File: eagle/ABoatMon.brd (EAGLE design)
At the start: 78.7 x 61 mm, 29 parts, among them J1 5V, J2 GND, J3 GND, J4 5V, X1 MKDSN1,5/3-5,08, X6 MKDSN1,5/3-5,08

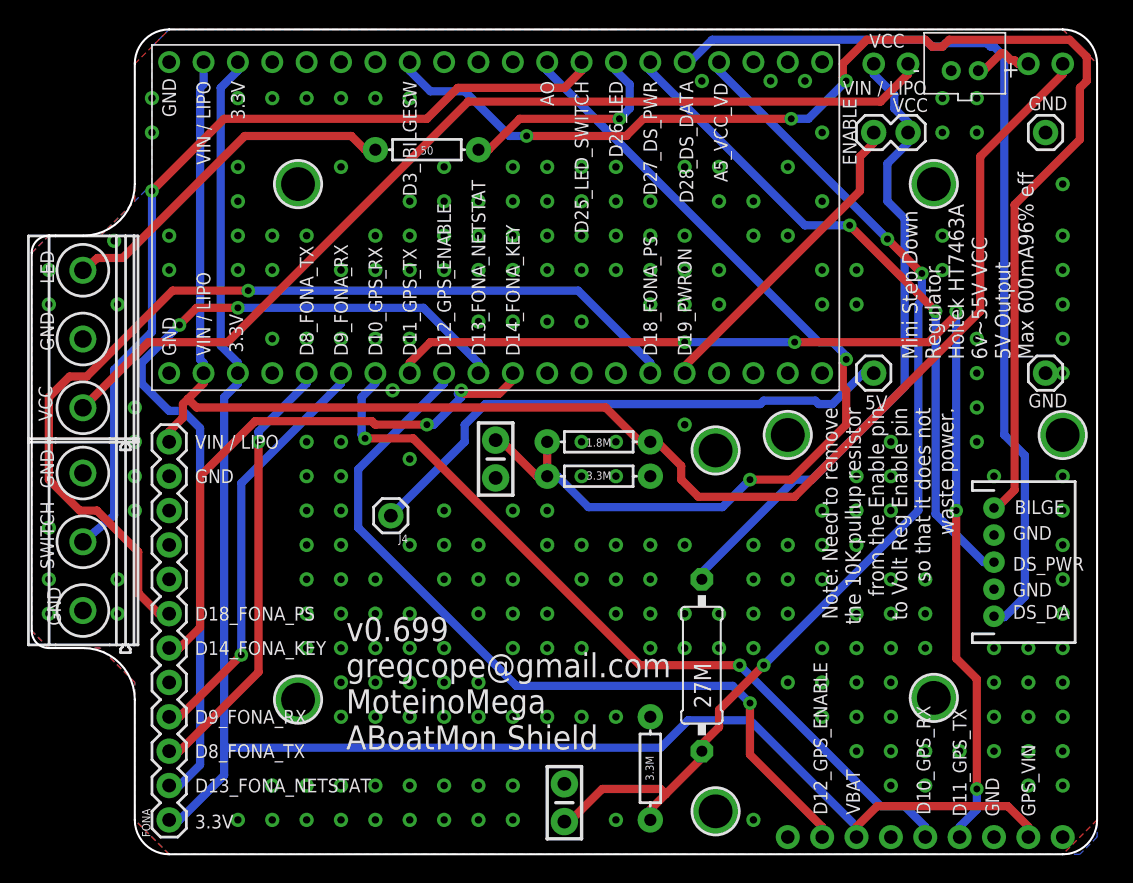
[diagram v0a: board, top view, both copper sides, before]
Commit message: Moved boxmounting holes 3mm
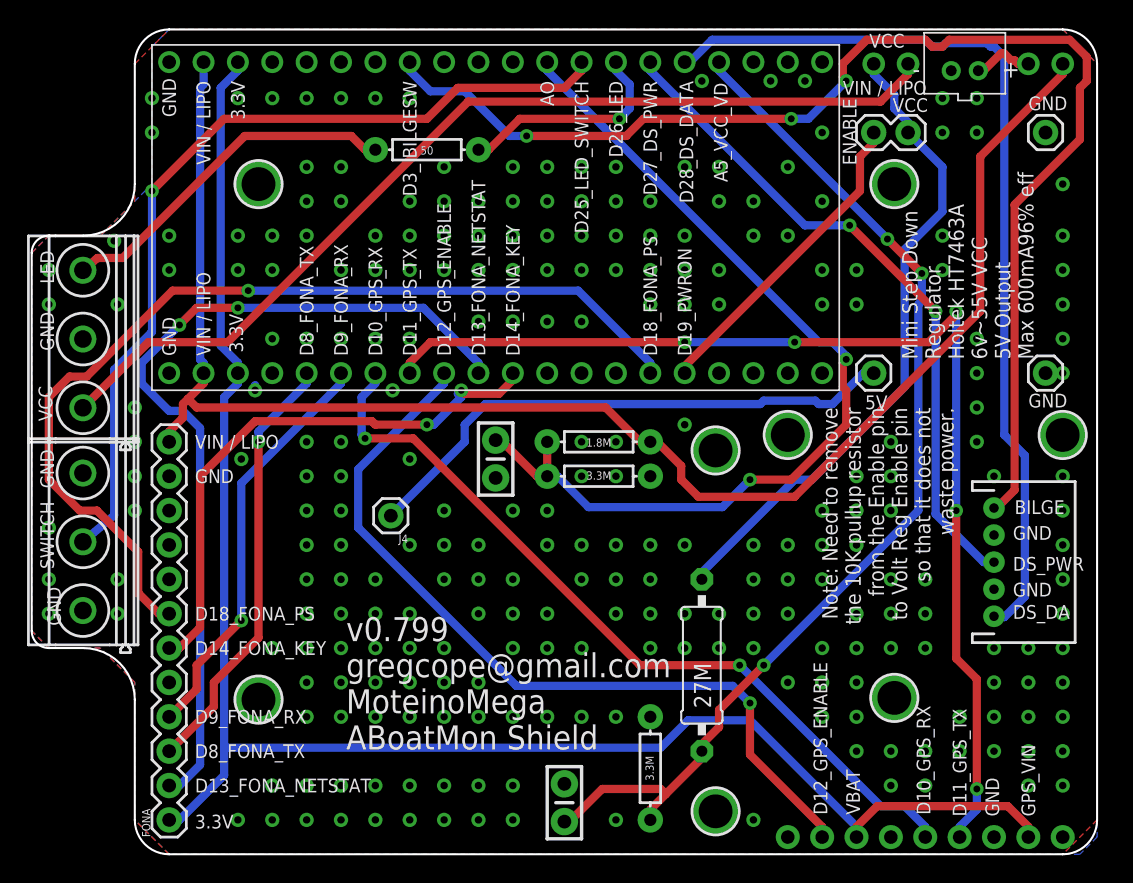
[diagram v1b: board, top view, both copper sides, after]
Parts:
- moved U$1 2.92 mm to (18.0, 11.4)
- moved U$6 2.92 mm to (18.0, 49.5)
- moved U$7 2.92 mm to (65.0, 49.5)
- moved U$8 2.92 mm to (65.0, 11.6)
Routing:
- net VCC_JUMPER: track 47.3 -> 48.3 mm
- net GND: track 0.00 -> 0.38 mm, vias 258 -> 257
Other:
- board text added: "v0.799 gregcope@gmail.com MoteinoMega ABoatMon Shield"
- board text removed: "v0.699 gregcope@gmail.com MoteinoMega ABoatMon Shield"
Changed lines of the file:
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@@
 <dimension x1="63.5" y1="35.56" x2="76.2" y2="35.56" x3="69.85" y3="34.29" textsize="1.778" layer="25"/>
 <dimension x1="63.5" y1="35.56" x2="63.5" y2="53.34" x3="63.881" y3="44.45" textsize="1.778" layer="25"/>
-<text x="24.511" y="7.747" size="1.778" layer="25">v0.699
+<text x="24.511" y="7.747" size="1.778" layer="25">v0.799
 gregcope@gmail.com
 MoteinoMega
@@
 <wire x1="77.47" y1="0" x2="80.01" y2="2.54" width="0.1524" layer="20" curve="90"/>
 <text x="73.787" y="19.05" size="1.016" layer="25" font="vector" ratio="20">GND</text>
+<dimension x1="20.955" y1="49.53" x2="18.034" y2="49.53" x3="19.4945" y3="9.779" textsize="1.778" layer="25"/>
 </plain>
 <attributes>
@@
 <attribute name="VALUE" x="74.803" y="23.241" size="0.6096" layer="27" font="vector" ratio="20" rot="R270"/>
 </element>
-<element name="U$1" library="microbuilder" package="MOUNTINGHOLE_2.5_PLATED" value="MOUNTINGHOLE2.5" x="20.955" y="11.43" smashed="yes"/>
-<element name="U$6" library="microbuilder" package="MOUNTINGHOLE_2.5_PLATED" value="MOUNTINGHOLE2.5" x="20.955" y="49.53" smashed="yes"/>
-<element name="U$7" library="microbuilder" package="MOUNTINGHOLE_2.5_PLATED" value="MOUNTINGHOLE2.5" x="67.945" y="49.53" smashed="yes"/>
-<element name="U$8" library="microbuilder" package="MOUNTINGHOLE_2.5_PLATED" value="MOUNTINGHOLE2.5" x="67.945" y="11.557" smashed="yes"/>
+<element name="U$1" library="microbuilder" package="MOUNTINGHOLE_2.5_PLATED" value="MOUNTINGHOLE2.5" x="18.034" y="11.43" smashed="yes"/>
+<element name="U$6" library="microbuilder" package="MOUNTINGHOLE_2.5_PLATED" value="MOUNTINGHOLE2.5" x="18.034" y="49.53" smashed="yes"/>
+<element name="U$7" library="microbuilder" package="MOUNTINGHOLE_2.5_PLATED" value="MOUNTINGHOLE2.5" x="65.024" y="49.53" smashed="yes"/>
+<element name="U$8" library="microbuilder" package="MOUNTINGHOLE_2.5_PLATED" value="MOUNTINGHOLE2.5" x="65.024" y="11.557" smashed="yes"/>
 </elements>
 <signals>
@@
 <via x="7.62" y="20.32" extent="1-16" drill="0.55"/>
 <via x="11.43" y="45.72" extent="1-16" drill="0.55"/>
-<via x="16.51" y="50.8" extent="1-16" drill="0.55"/>
-<via x="16.51" y="48.26" extent="1-16" drill="0.55"/>
 <via x="16.51" y="45.72" extent="1-16" drill="0.55"/>
 <via x="16.51" y="43.18" extent="1-16" drill="0.55"/>
@@
 <via x="59.69" y="12.7" extent="1-16" drill="0.55"/>
 <via x="62.23" y="12.7" extent="1-16" drill="0.55"/>
-<via x="64.77" y="12.7" extent="1-16" drill="0.55"/>
 <via x="59.69" y="10.16" extent="1-16" drill="0.55"/>
 <via x="62.23" y="10.16" extent="1-16" drill="0.55"/>
-<via x="64.77" y="10.16" extent="1-16" drill="0.55"/>
 <via x="62.23" y="7.62" extent="1-16" drill="0.55"/>
 <via x="64.77" y="7.62" extent="1-16" drill="0.55"/>
@@
 <via x="71.12" y="33.02" extent="1-16" drill="0.55"/>
 <via x="71.12" y="30.48" extent="1-16" drill="0.55"/>
-<wire x1="27.94" y1="34.29" x2="26.67" y2="38.1" width="0" layer="19" extent="1-1"/>
+<via x="69.85" y="10.16" extent="1-16" drill="0.55"/>
+<via x="17.78" y="34.29" extent="1-16" drill="0.55"/>
+<via x="16.764" y="29.21" extent="1-16" drill="0.55"/>
+<wire x1="17.78" y1="34.29" x2="17.78" y2="34.6747375" width="0.6096" layer="16"/>
+<wire x1="17.78" y1="34.6747375" x2="17.78" y2="34.6747375" width="0.6096" layer="16"/>
+<wire x1="17.78" y1="34.6747375" x2="19.05" y2="38.1" width="0" layer="19" extent="16-16"/>
 </signal>
 <signal name="VIN" class="1">
@@
 <contactref element="FONA" pad="4"/>
 <wire x1="24.13" y1="34.798" x2="24.13" y2="35.56" width="0.6096" layer="16"/>
-<wire x1="16.764" y1="27.432" x2="24.13" y2="34.798" width="0.6096" layer="16"/>
-<wire x1="16.764" y1="14.732" x2="16.764" y2="27.432" width="0.6096" layer="16"/>
-<wire x1="12.192" y1="10.16" x2="16.764" y2="14.732" width="0.6096" layer="1"/>
-<wire x1="11.43" y1="10.16" x2="12.192" y2="10.16" width="0.6096" layer="1"/>
-<via x="16.764" y="14.732" extent="1-16" drill="0.508"/>
+<wire x1="24.13" y1="34.798" x2="16.764" y2="27.432" width="0.6096" layer="16"/>
+<wire x1="16.764" y1="17.272" x2="13.462" y2="13.97" width="0.6096" layer="1"/>
+<wire x1="13.462" y1="13.97" x2="13.462" y2="12.192" width="0.6096" layer="1"/>
+<wire x1="11.43" y1="10.16" x2="13.462" y2="12.192" width="0.6096" layer="1"/>
+<via x="16.764" y="17.272" extent="1-16" drill="0.508"/>
+<wire x1="16.764" y1="27.432" x2="16.764" y2="17.272" width="0.6096" layer="16"/>
 </signal>
 <signal name="D8_FONA_TX">
@@
 <wire x1="18.034" y1="31.242" x2="21.59" y2="34.798" width="0.6096" layer="16"/>
 <wire x1="18.034" y1="30.48" x2="18.034" y2="31.242" width="0.6096" layer="16"/>
-<wire x1="18.034" y1="13.462" x2="18.034" y2="30.48" width="0.6096" layer="1"/>
-<wire x1="12.192" y1="7.62" x2="18.034" y2="13.462" width="0.6096" layer="1"/>
-<wire x1="11.43" y1="7.62" x2="12.192" y2="7.62" width="0.6096" layer="1"/>
+<wire x1="18.034" y1="16.002" x2="18.034" y2="30.48" width="0.6096" layer="1"/>
+<wire x1="18.034" y1="16.002" x2="14.732" y2="12.7" width="0.6096" layer="1"/>
+<wire x1="14.732" y1="12.7" x2="14.732" y2="10.922" width="0.6096" layer="1"/>
+<wire x1="11.43" y1="7.62" x2="14.732" y2="10.922" width="0.6096" layer="1"/>
 <via x="18.034" y="30.48" extent="1-16" drill="0.508"/>
 </signal>
@@
 <wire x1="58.928" y1="27.686" x2="57.658" y2="27.686" width="0.6096" layer="16"/>
 <wire x1="65.786" y1="34.544" x2="58.928" y2="27.686" width="0.6096" layer="16"/>
-<wire x1="65.786" y1="46.99" x2="65.786" y2="34.544" width="0.6096" layer="16"/>
-<wire x1="64.516" y1="48.26" x2="65.786" y2="46.99" width="0.6096" layer="16"/>
-<wire x1="64.516" y1="51.054" x2="64.516" y2="48.26" width="0.6096" layer="16"/>
-<wire x1="66.04" y1="52.578" x2="64.516" y2="51.054" width="0.6096" layer="16"/>
-<wire x1="66.04" y1="53.34" x2="66.04" y2="52.578" width="0.6096" layer="16"/>
+<wire x1="65.786" y1="44.704" x2="65.786" y2="34.544" width="0.6096" layer="16"/>
+<wire x1="68.58" y1="47.498" x2="65.786" y2="44.704" width="0.6096" layer="16"/>
+<wire x1="66.04" y1="53.34" x2="68.58" y2="50.8" width="0.6096" layer="16"/>
+<wire x1="68.58" y1="50.8" x2="68.58" y2="47.498" width="0.6096" layer="16"/>
 <wire x1="63.5" y1="57.658" x2="63.5" y2="58.42" width="0.6096" layer="16"/>
 <wire x1="65.024" y1="56.134" x2="63.5" y2="57.658" width="0.6096" layer="16"/>
@@
 <wire x1="74.93" y1="58.42" x2="74.168" y2="58.42" width="0.6096" layer="1"/>
 </signal>
+<signal name="GND1" class="1">
+<via x="21.59" y="48.26" extent="1-16" drill="0.55"/>
+</signal>
+<signal name="GND2" class="1">
+<via x="21.59" y="50.8" extent="1-16" drill="0.55"/>
+</signal>
+<signal name="GND3" class="1">
+<via x="24.13" y="48.26" extent="1-16" drill="0.55"/>
+</signal>
+<signal name="GND4" class="1">
+<via x="21.59" y="12.7" extent="1-16" drill="0.55"/>
+</signal>
+<signal name="GND5" class="1">
+<via x="21.59" y="10.16" extent="1-16" drill="0.55"/>
+</signal>
+<signal name="GND6" class="1">
+<via x="19.05" y="15.24" extent="1-16" drill="0.55"/>
+</signal>
 </signals>

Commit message: starting again
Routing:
- net GND: vias 257 -> 263
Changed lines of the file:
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@@
 <wire x1="17.78" y1="34.29" x2="17.78" y2="34.6747375" width="0.6096" layer="16"/>
 <wire x1="17.78" y1="34.6747375" x2="17.78" y2="34.6747375" width="0.6096" layer="16"/>
+<via x="21.59" y="50.8" extent="1-16" drill="0.55"/>
+<via x="21.59" y="48.26" extent="1-16" drill="0.55"/>
+<via x="24.13" y="48.26" extent="1-16" drill="0.55"/>
+<via x="19.05" y="15.24" extent="1-16" drill="0.55"/>
+<via x="21.59" y="12.7" extent="1-16" drill="0.55"/>
+<via x="21.59" y="10.16" extent="1-16" drill="0.55"/>
+<wire x1="21.59" y1="12.7" x2="21.59" y2="10.16" width="0" layer="19" extent="1-1"/>
 <wire x1="17.78" y1="34.6747375" x2="19.05" y2="38.1" width="0" layer="19" extent="16-16"/>
 </signal>
@@
 <wire x1="74.93" y1="58.42" x2="74.168" y2="58.42" width="0.6096" layer="1"/>
 </signal>
-<signal name="GND1" class="1">
-<via x="21.59" y="48.26" extent="1-16" drill="0.55"/>
-</signal>
-<signal name="GND2" class="1">
-<via x="21.59" y="50.8" extent="1-16" drill="0.55"/>
-</signal>
-<signal name="GND3" class="1">
-<via x="24.13" y="48.26" extent="1-16" drill="0.55"/>
-</signal>
-<signal name="GND4" class="1">
-<via x="21.59" y="12.7" extent="1-16" drill="0.55"/>
-</signal>
-<signal name="GND5" class="1">
-<via x="21.59" y="10.16" extent="1-16" drill="0.55"/>
-</signal>
-<signal name="GND6" class="1">
-<via x="19.05" y="15.24" extent="1-16" drill="0.55"/>
-</signal>
 </signals>

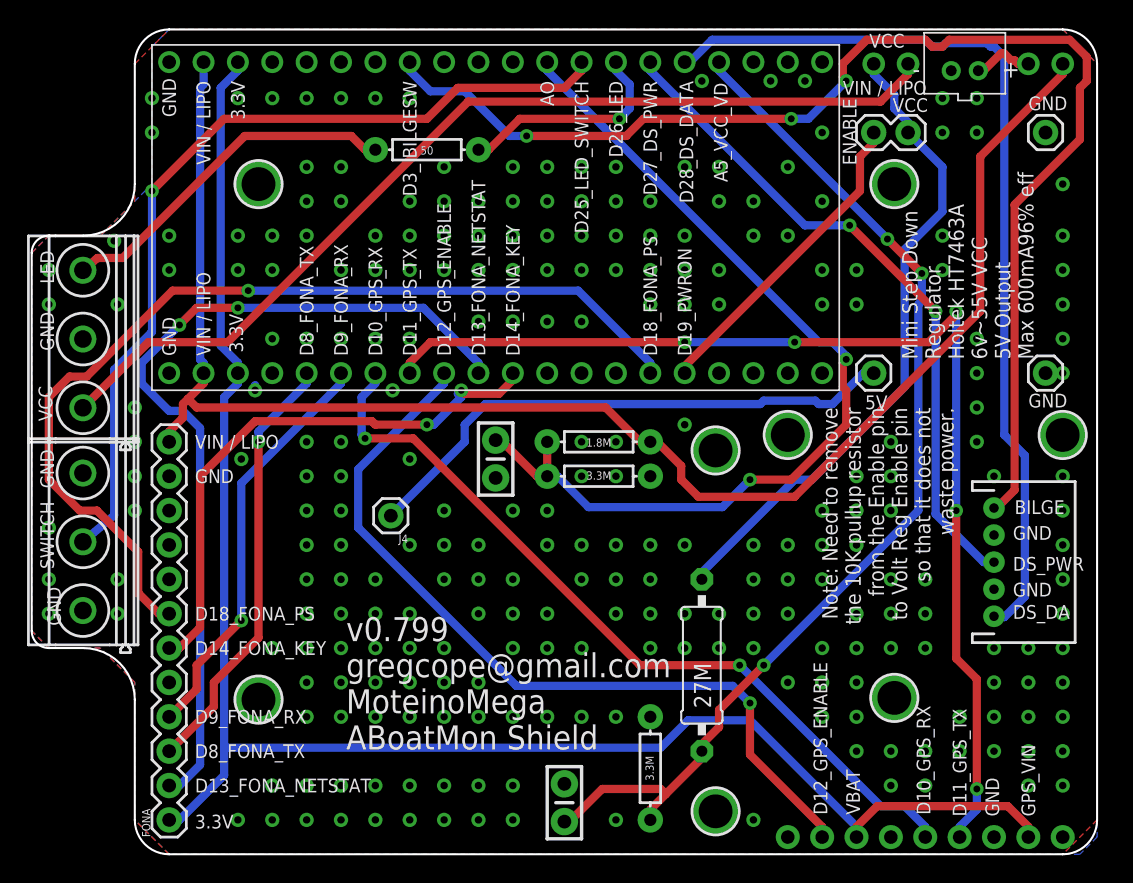
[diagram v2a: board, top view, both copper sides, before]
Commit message: bigger JST, added 4.7K
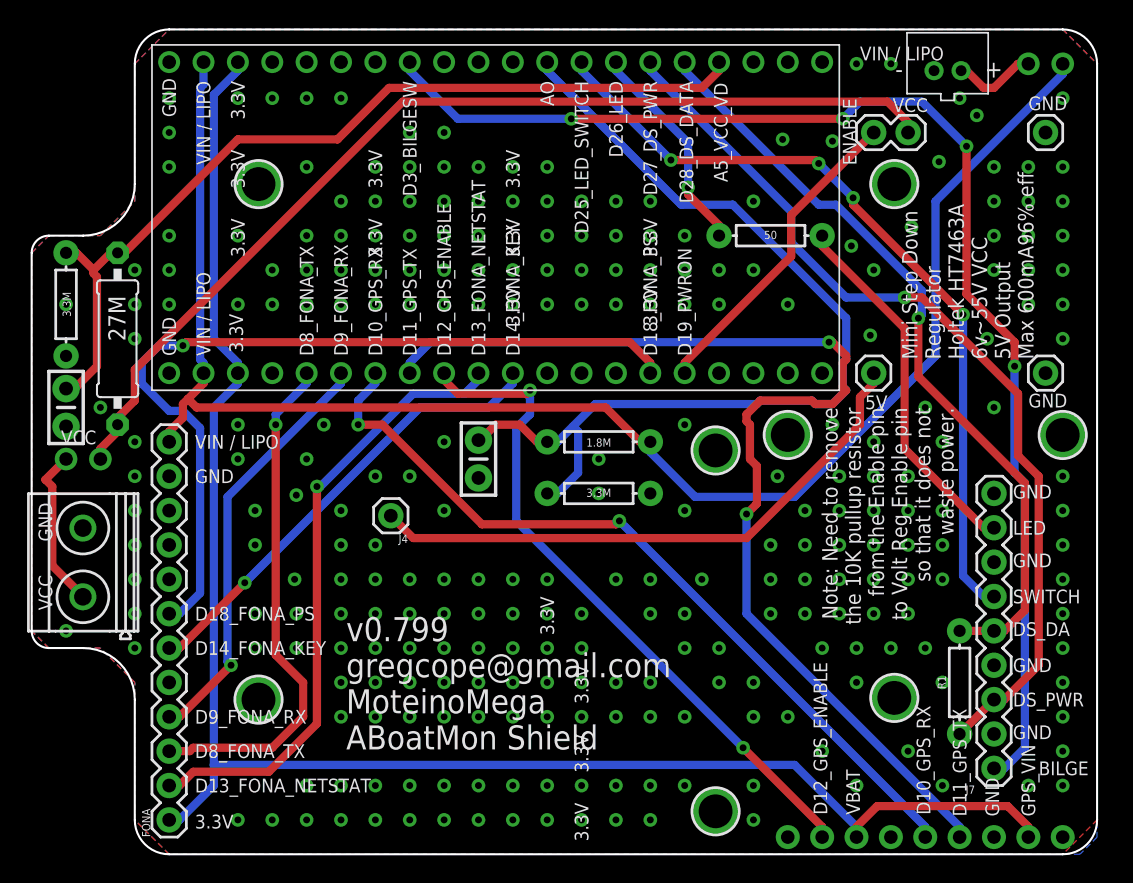
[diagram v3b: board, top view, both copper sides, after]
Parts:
- removed J6: (no value), SparkFun-Connectors:JST-5-PTH
- removed X6: MKDSN1,5/3-5,08, con-phoenix-508:MKDSN1,5/3-5,08
- added J7: (no value), SparkFun-Connectors:1X09
- added R1: 4.7K, SparkFun-Resistors:AXIAL-0.3
- X1: value MKDSN1,5/3-5,08 -> MKDSN1,5/2-5,08; device con-phoenix-508:MKDSN1,5/3-5,08 -> con-phoenix-508:MKDSN1,5/2-5,08
- moved VCC 66.5 mm to (5.08, 29.2), turned to 180 degrees
- moved R5 55.1 mm to (3.81, 40.6), turned to 90 degrees
- moved R6 49.5 mm to (7.62, 38.1), turned to 270 degrees
- moved C2 47.0 mm to (3.81, 33.0), turned to 270 degrees
- moved R7 26.2 mm to (55.9, 45.7), turned to 180 degrees
- moved X1 4.06 mm to (5.08, 21.6)
- moved C1 1.27 mm to (34.3, 29.2)
- moved R3 1.27 mm to (43.2, 26.7)
- moved JST1 1.27 mm to (69.0, 57.9)
- renumbered U$6 to GND
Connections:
- net D25_LED_SWITCH: now also J7.6; no longer X1.2
- net D27_DS_PWR: now also J7.3, R1.P$1; no longer J6.3
- net D28_DS_DATA: now also J7.5, R1.P$2; no longer J6.5
- net D3_BILGESW: now also J7.1; no longer J6.1
- net GND: now also J7.2, J7.4, J7.7, J7.9, X1.2; no longer J6.2, J6.4, X1.1, X1.3, X6.2
- net LED: now also J7.8; no longer X6.3
- net VCC: now also X1.1; no longer X6.1
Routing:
- net VCC: track 72.0 -> 12.0 mm
- net VCC_JUMPER: track 48.3 -> 74.4 mm
- net D13_FONA_NETSTAT: track 64.0 -> 46.0 mm, vias 2 -> 1
- net D27_DS_PWR: track 49.9 -> 67.7 mm, vias 2 -> 1
- net A5_VCC_VD: track 79.3 -> 65.8 mm, vias 3 -> 0
- net D28_DS_DATA: track 68.6 -> 57.3 mm, vias 0 -> 1
- net D12_GPS_ENABLE: track 60.5 -> 50.4 mm, vias 1 -> 2
- net D18_FONA_PS: track 71.6 -> 61.9 mm
- net D14_FONA_KEY: track 41.6 -> 34.3 mm, vias 2 -> 1
- net D8_FONA_TX: track 32.1 -> 38.1 mm
- net D25_LED_SWITCH: track 64.2 -> 58.8 mm, vias 1 -> 4
- net A0: track 69.9 -> 72.4 mm, vias 2 -> 0
- net 5V: track 41.0 -> 43.1 mm
- net VIN_JUMPER: track 4.54 -> 6.23 mm
- net LED: track 26.1 -> 27.3 mm
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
